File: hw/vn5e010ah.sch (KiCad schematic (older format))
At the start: 3 parts, among them U1001 VN5E010AH

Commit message: 1.0 pcb created
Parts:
- R1001: symbol 390 -> yageo:390
- R502: symbol 1K -> yageo:1K
- U1001: symbol VN5E010AH -> usevolt:VN5E010AH
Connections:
- wire segments 16 -> 21
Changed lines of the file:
@@
-EESchema Schematic File Version 2
-LIBS:esb-rescue
-LIBS:kemet
-LIBS:usevolt
-LIBS:wurth_elektronik_LED
-LIBS:power
-LIBS:yageo
-LIBS:esb-cache
+EESchema Schematic File Version 4
+LIBS:hcu-cache
 EELAYER 26 0
 EELAYER END
 $Descr A4 11693 8268
 encoding utf-8
-Sheet 8 13
+Sheet 14 15
 Title ""
 Date ""
@@
 SENSE1
 Wire Wire Line
-	4350 3300 4900 3300
+	4350 3300 4600 3300
 Wire Wire Line
 	3850 3300 4050 3300
 Wire Wire Line
-	3450 3200 4900 3200
+	3450 3200 3600 3200
 Wire Wire Line
 	4350 3800 4600 3800
 $Comp
-L VDD #PWR602
+L power:VDD #PWR602
 U 1 1 59D7E637
 P 4600 3000
@@
 AR Path="/5A13680F/59D7E637" Ref="#PWR048"  Part="1"
 AR Path="/5A14370A/59D7E637" Ref="#PWR051"  Part="1"
-F 0 "#PWR051" H 4600 2850 50  0001 C CNN
+AR Path="/5ABCCFA7/59D7E637" Ref="#PWR0107"  Part="1"
+F 0 "#PWR0107" H 4600 2850 50  0001 C CNN
 F 1 "VDD" H 4617 3173 50  0000 C CNN
 F 2 "" H 4600 3000 50  0000 C CNN
@@
 	5700 3300 5700 3200
 Wire Wire Line
-	5600 3200 6200 3200
+	5600 3200 5700 3200
 Connection ~ 5700 3200
 Wire Wire Line
@@
 Connection ~ 4600 3300
 $Comp
-L GND #PWR601
+L power:GND #PWR601
 U 1 1 5A014ACD
 P 3850 3600
@@
 AR Path="/5A13680F/5A014ACD" Ref="#PWR049"  Part="1"
 AR Path="/5A14370A/5A014ACD" Ref="#PWR052"  Part="1"
-F 0 "#PWR052" H 3850 3350 50  0001 C CNN
+AR Path="/5ABCCFA7/5A014ACD" Ref="#PWR0108"  Part="1"
+F 0 "#PWR0108" H 3850 3350 50  0001 C CNN
 F 1 "GND" H 3855 3427 50  0000 C CNN
 F 2 "" H 3850 3600 50  0000 C CNN
@@
 $EndComp
 Wire Wire Line
-	3850 3300 3850 3600
-$Comp
-L 1K R502
+	3850 3300 3850 3550
+$Comp
+L yageo:1K R502
 U 1 1 5A058D94
 P 3600 3350
@@
 AR Path="/5A13680F/5A058D94" Ref="R1502"  Part="1"
 AR Path="/5A14370A/5A058D94" Ref="R1602"  Part="1"
-F 0 "R801" V 3608 3408 45  0000 L CNN
+AR Path="/5ABCCFA7/5A058D94" Ref="R1403"  Part="1"
+F 0 "R1403" V 3608 3408 45  0000 L CNN
 F 1 "1K" V 3692 3408 45  0000 L CNN
 F 2 "yageo:0603" H 3630 3500 20  0001 C CNN
@@
 Connection ~ 3850 3550
 $Comp
-L 390 R1001
+L yageo:390 R1001
 U 1 1 5A32CF0E
 P 4150 3300
@@
 AR Path="/5A1358B0/5A32CF0E" Ref="R1101"  Part="1"
 AR Path="/5A13680F/5A32CF0E" Ref="R1202"  Part="1"
-F 0 "R802" H 4200 3484 45  0000 C CNN
+AR Path="/5ABCCFA7/5A32CF0E" Ref="R1404"  Part="1"
+F 0 "R1404" H 4200 3484 45  0000 C CNN
 F 1 "390" H 4200 3400 45  0000 C CNN
 F 2 "yageo:0603" H 4180 3450 20  0001 C CNN
@@
 $EndComp
 $Comp
-L VN5E010AH U1001
+L usevolt:VN5E010AH U1001
 U 1 1 5A32CF4A
 P 5300 3300
@@
 AR Path="/5A1358B0/5A32CF4A" Ref="U1101"  Part="1"
 AR Path="/5A13680F/5A32CF4A" Ref="U1201"  Part="1"
-F 0 "U801" H 5250 3747 60  0000 C CNN
+AR Path="/5ABCCFA7/5A32CF4A" Ref="U1401"  Part="1"
+F 0 "U1401" H 5250 3747 60  0000 C CNN
 F 1 "VN5E010AH" H 5250 3641 60  0000 C CNN
 F 2 "usevolt:HPAK" H 4950 4250 60  0001 C CNN
@@
 $EndComp
 $Comp
-L GND #PWR044
+L power:GND #PWR044
 U 1 1 5A32CF90
 P 4800 3600
@@
 AR Path="/5A1358B0/5A32CF90" Ref="#PWR047"  Part="1"
 AR Path="/5A13680F/5A32CF90" Ref="#PWR050"  Part="1"
-F 0 "#PWR053" H 4800 3350 50  0001 C CNN
+AR Path="/5ABCCFA7/5A32CF90" Ref="#PWR0109"  Part="1"
+F 0 "#PWR0109" H 4800 3350 50  0001 C CNN
 F 1 "GND" H 4805 3427 50  0000 C CNN
 F 2 "" H 4800 3600 50  0000 C CNN
@@
 $EndComp
 Wire Wire Line
-	4800 3400 4800 3600
+	4800 3400 4800 3500
 Wire Wire Line
 	4800 3500 4900 3500
@@
 	4900 3400 4800 3400
 Connection ~ 4800 3500
+Wire Wire Line
+	5700 3200 6200 3200
+Wire Wire Line
+	4600 3300 4900 3300
+Wire Wire Line
+	3600 3200 4900 3200
+Wire Wire Line
+	3850 3550 3850 3600
+Wire Wire Line
+	4800 3500 4800 3600
 $EndSCHEMATC

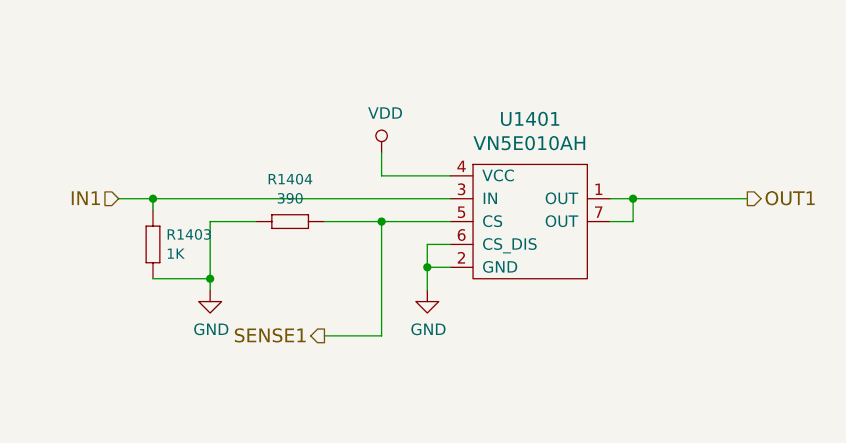
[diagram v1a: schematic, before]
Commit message: pull down resistor and flyback diode added to out11
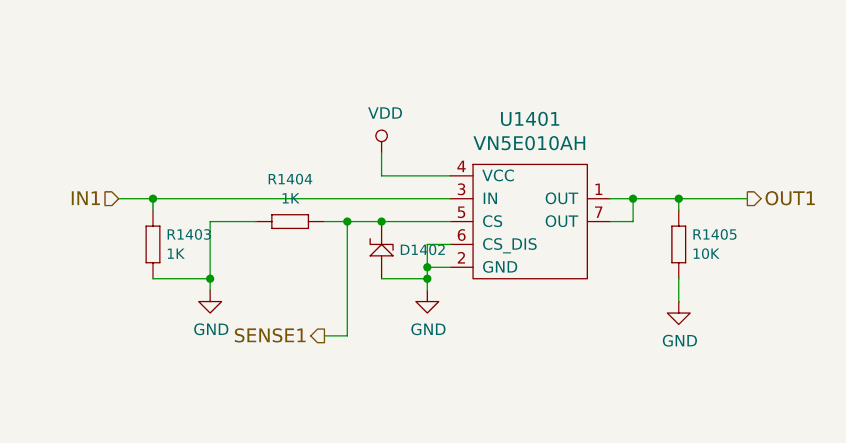
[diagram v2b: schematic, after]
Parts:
- removed R1001: 390, yageo:0603, symbol yageo:390
- added D1402: ZENER_MM3Z3V6T1G, usevolt:SOD-323, symbol usevolt:ZENER_MM3Z3V6T1G
- added R1404: 1K, yageo:0603, symbol yageo:1K
- added R1405: 10K, yageo:0603, symbol yageo:10K
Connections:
- net GND: now also D1402.2, R1404.2 (R2), R1405.1 (R1)
- net OUT1: now also R1405.2 (R2)
- net SENSE1: now also D1402.1, R1404.1 (R1)
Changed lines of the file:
@@
 SENSE1
 Wire Wire Line
-	4350 3300 4600 3300
+	4350 3300 4450 3300
 Wire Wire Line
 	3850 3300 4050 3300
@@
 	3450 3200 3600 3200
 Wire Wire Line
-	4350 3800 4600 3800
+	4350 3800 4450 3800
 $Comp
 L power:VDD #PWR602
@@
 	4600 3000 4600 3100
 Wire Wire Line
-	4600 3800 4600 3300
-Connection ~ 4600 3300
+	4450 3800 4450 3300
+Connection ~ 4450 3300
 $Comp
 L power:GND #PWR601
@@
 Connection ~ 3850 3550
 $Comp
-L yageo:390 R1001
-U 1 1 5A32CF0E
-P 4150 3300
-AR Path="/5A1349CF/5A32CF0E" Ref="R1001"  Part="1"
-AR Path="/5A14370A/5A32CF0E" Ref="R1302"  Part="1"
-AR Path="/5A120DD2/5A32CF0E" Ref="R601"  Part="1"
-AR Path="/5A12FF64/5A32CF0E" Ref="R802"  Part="1"
-AR Path="/5A130D3E/5A32CF0E" Ref="R902"  Part="1"
-AR Path="/5A1358B0/5A32CF0E" Ref="R1101"  Part="1"
-AR Path="/5A13680F/5A32CF0E" Ref="R1202"  Part="1"
-AR Path="/5ABCCFA7/5A32CF0E" Ref="R1404"  Part="1"
-F 0 "R1404" H 4200 3484 45  0000 C CNN
-F 1 "390" H 4200 3400 45  0000 C CNN
-F 2 "yageo:0603" H 4180 3450 20  0001 C CNN
-F 3 "" H 4119 3339 60  0001 C CNN
-F 4 "" H 4519 3739 60  0001 C CNN "1st Source Part Number"
-F 5 "Digikey" H 4419 3639 60  0001 C CNN "1st Source"
-F 6 "RC0603FR-07390RL" H 4319 3539 60  0001 C CNN "Manufacturer Part Number"
-F 7 "YAGEO" H 4219 3439 60  0001 C CNN "Manufacturer"
-	1    4150 3300
-	1    0    0    -1
-$EndComp
-$Comp
 L usevolt:VN5E010AH U1001
 U 1 1 5A32CF4A
@@
 Connection ~ 4800 3500
 Wire Wire Line
-	5700 3200 6200 3200
+	5700 3200 5900 3200
+Wire Wire Line
+	4450 3300 4600 3300
+Wire Wire Line
+	3600 3200 4900 3200
+Wire Wire Line
+	3850 3550 3850 3600
+Wire Wire Line
+	4800 3500 4800 3550
+$Comp
+L yageo:10K R1405
+U 1 1 5B6FF483
+P 5900 3350
+F 0 "R1405" V 5908 3408 45  0000 L CNN
+F 1 "10K" V 5992 3408 45  0000 L CNN
+F 2 "yageo:0603" H 5930 3500 20  0001 C CNN
+F 3 "" H 5869 3389 60  0001 C CNN
+F 4 "" H 6269 3789 60  0001 C CNN "1st Source Part Number"
+F 5 "Digikey" H 6169 3689 60  0001 C CNN "1st Source"
+F 6 "RC0603FR-0710KL" H 6069 3589 60  0001 C CNN "Manufacturer Part Number"
+F 7 "YAGEO" H 5969 3489 60  0001 C CNN "Manufacturer"
+	1    5900 3350
+	0    1    1    0
+$EndComp
+Wire Wire Line
+	5900 3250 5900 3200
+Connection ~ 5900 3200
+Wire Wire Line
+	5900 3200 6200 3200
+$Comp
+L power:GND #PWR0110
+U 1 1 5B6FF6EF
+P 5900 3650
+F 0 "#PWR0110" H 5900 3400 50  0001 C CNN
+F 1 "GND" H 5905 3477 50  0000 C CNN
+F 2 "" H 5900 3650 50  0000 C CNN
+F 3 "" H 5900 3650 50  0000 C CNN
+	1    5900 3650
+	1    0    0    -1
+$EndComp
+Wire Wire Line
+	5900 3650 5900 3550
+$Comp
+L yageo:1K R1404
+U 1 1 5B7000FE
+P 4150 3300
+F 0 "R1404" H 4200 3484 45  0000 C CNN
+F 1 "1K" H 4200 3400 45  0000 C CNN
+F 2 "yageo:0603" H 4180 3450 20  0001 C CNN
+F 3 "" H 4119 3339 60  0001 C CNN
+F 4 "" H 4519 3739 60  0001 C CNN "1st Source Part Number"
+F 5 "Digikey" H 4419 3639 60  0001 C CNN "1st Source"
+F 6 "RC0603FR-071KL" H 4319 3539 60  0001 C CNN "Manufacturer Part Number"
+F 7 "YAGEO" H 4219 3439 60  0001 C CNN "Manufacturer"
+	1    4150 3300
+	1    0    0    -1
+$EndComp
+$Comp
+L usevolt:ZENER_MM3Z3V6T1G D1402
+U 1 1 5B7009B4
+P 4600 3350
+F 0 "D1402" V 4525 3272 45  0000 R CNN
+F 1 "ZENER_MM3Z3V6T1G" H 4875 3725 45  0001 L BNN
+F 2 "usevolt:SOD-323" H 4575 3725 20  0001 C CNN
+F 3 "http://www.mouser.com/ds/2/308/MM3Z2V4T1-D-269162.pdf" H 4950 3925 60  0001 C CNN
+F 4 "Mouser" H 4920 3670 60  0001 C CNN "1st Source"
+F 5 "MM3Z3V6T1G" H 4820 3570 60  0001 C CNN "Manufacturer Part Number"
+F 6 "863-MM3Z3V6T1G" H 5020 3770 60  0001 C CNN "1st Source Part Number"
+F 7 "ON Semiconductor" H 4875 3825 60  0001 C CNN "Manufacturer"
+	1    4600 3350
+	0    -1   -1   0
+$EndComp
+Connection ~ 4600 3300
 Wire Wire Line
 	4600 3300 4900 3300
 Wire Wire Line
-	3600 3200 4900 3200
-Wire Wire Line
-	3850 3550 3850 3600
-Wire Wire Line
-	4800 3500 4800 3600
+	4600 3550 4800 3550
+Connection ~ 4800 3550
+Wire Wire Line
+	4800 3550 4800 3600
 $EndSCHEMATC
